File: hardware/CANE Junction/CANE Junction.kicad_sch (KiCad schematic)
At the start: 19 parts, among them J101 Conn_02x05_Odd_Even, SW101 SW_Push, U101 NCP163ASN330T1G, U102 NCP163ASN330T1G, U103 XMSM0G3507SDGS28R

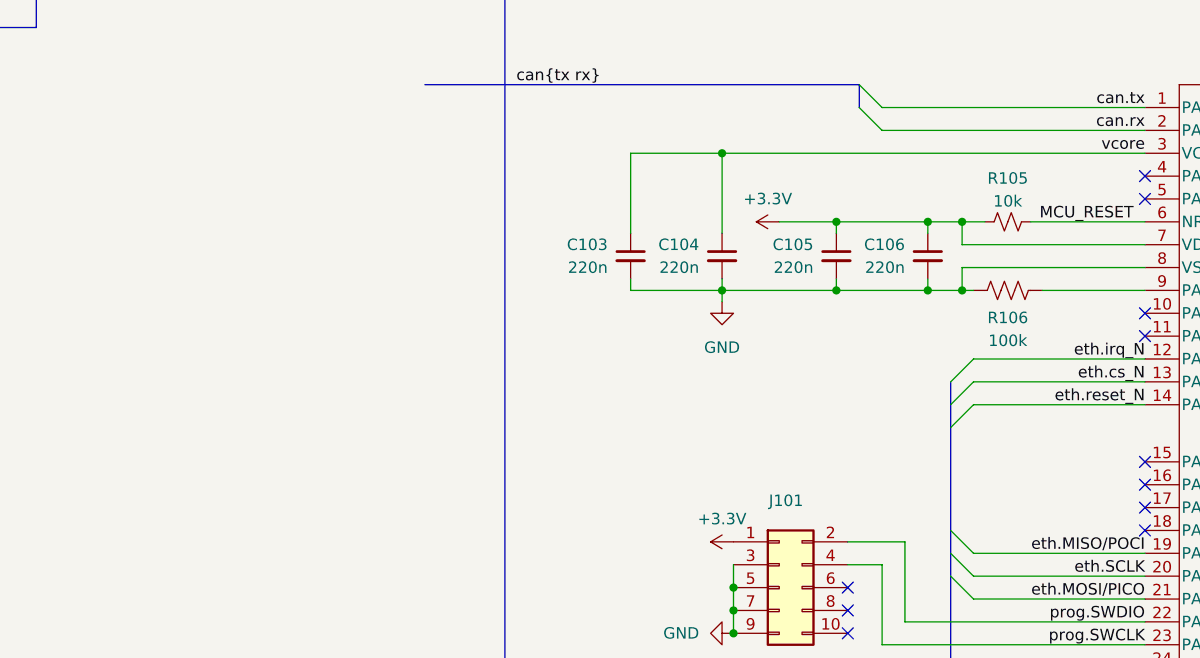
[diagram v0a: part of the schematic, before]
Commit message: pt
mspm0g3519 is da goat. 2 can interfaces but gate kept by bga footprint and high pin count qfps. one must manually port it. started the port, 2 out of 100 pins done :D :D u love ultra librariariairan
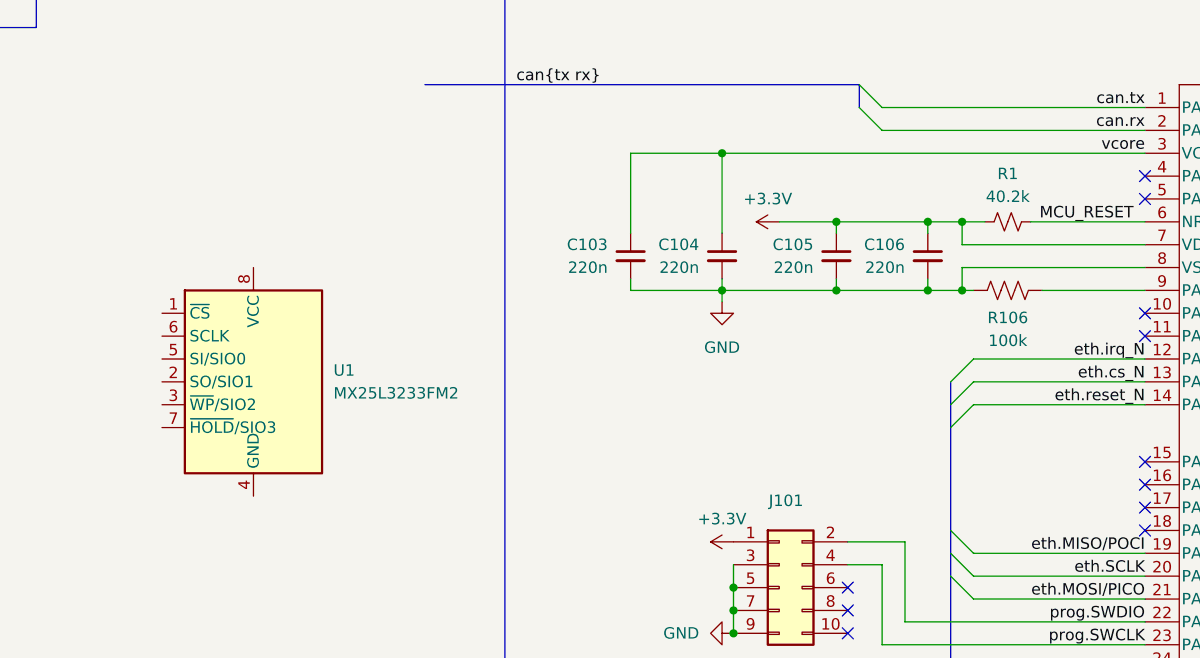
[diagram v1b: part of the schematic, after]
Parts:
- removed R105: 10k, Resistor_SMD:R_0805_2012Metric_Pad1.20x1.40mm_HandSolder, symbol Device:R_Small_US
- added R1: 40.2k, Resistor_SMD:R_0805_2012Metric_Pad1.20x1.40mm_HandSolder, symbol Device:R_Small_US
- added U1: MX25L3233FM2, Package_SO:SOIC-8_3.9x4.9mm_P1.27mm, symbol Memory_Flash:MX25L3233FM2
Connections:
- net +3.3V: now also R1.2
- net MCU_RESET: now also R1.1
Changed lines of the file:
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@@
+	(symbol
+		(lib_id "Device:R_Small_US")
+		(at 209.55 90.17 270)
+		(unit 1)
+		(exclude_from_sim no)
+		(in_bom yes)
+		(on_board yes)
+		(dnp no)
+		(property "Reference" "R1"
+			(at 209.55 84.836 90)
+			(effects
+				(font
+					(size 1.27 1.27)
+				)
+			)
+		)
+		(property "Value" "40.2k"
+			(at 209.55 87.376 90)
+			(effects
+				(font
+					(size 1.27 1.27)
+				)
+			)
+		)
+		(property "Footprint" "Resistor_SMD:R_0805_2012Metric_Pad1.20x1.40mm_HandSolder"
+			(at 209.55 90.17 0)
+			(effects
+				(font
+					(size 1.27 1.27)
+				)
+				(hide yes)
+			)
+		)
+		(property "Datasheet" ""
+			(at 209.55 90.17 0)
+			(effects
+				(font
+					(size 1.27 1.27)
+				)
+				(hide yes)
+			)
+		)
+		(property "Description" "Resistor, US symbol"
+			(at 209.55 90.17 0)
+			(effects
+				(font
+					(size 1.27 1.27)
+				)
+				(hide yes)
+			)
+		)
+		(property "mouser" "https://www.mouser.com/ProductDetail/KOA-Speer/RK73H2ATTD4022F?qs=sGAEpiMZZMvdGkrng054txknJuA7M8fa4wn7EqIHwNI%3D"
+			(at 209.55 90.17 0)
+			(effects
+				(font
+					(size 1.27 1.27)
+				)
+				(hide yes)
+			)
+		)
+		(property "specs" "40.2k ohm, 250mW, 1%, 150V, 100ppm, -55C, +155C"
+			(at 209.55 90.17 0)
+			(effects
+				(font
+					(size 1.27 1.27)
+				)
+				(hide yes)
+			)
+		)
+		(property "unit x10" "0.02"
+			(at 209.55 90.17 0)
+			(effects
+				(font
+					(size 1.27 1.27)
+				)
+				(hide yes)
+			)
+		)
+		(property "unit x1" "0.1"
+			(at 209.55 90.17 0)
+			(effects
+				(font
+					(size 1.27 1.27)
+				)
+				(hide yes)
+			)
+		)
+		(property "Mouser Part Number" ""
+			(at 209.55 90.17 0)
+			(effects
+				(font
+					(size 1.27 1.27)
+				)
+				(hide yes)
+			)
+		)
+		(property "Field10" ""
+			(at 209.55 90.17 0)
+			(effects
+				(font
+					(size 1.27 1.27)
+				)
+				(hide yes)
+			)
+		)
+		(pin "2"
+		)
+		(pin "1"
+		)
+		(instances
+			(project "CANE Junction"
+				(path "/20ac6af0-79b5-4ba6-aad3-75081d02c913"
+					(reference "R1")
+					(unit 1)
+				)
+			)
+		)
+	)
 	(symbol
 		(lib_id "Device:R_Small_US")
@@
 	)
 	(symbol
-		(lib_id "Device:R_Small_US")
-		(at 209.55 90.17 270)
+		(lib_id "Memory_Flash:MX25L3233FM2")
+		(at 125.73 107.95 0)
 		(unit 1)
 		(exclude_from_sim no)
@@
 		(on_board yes)
 		(dnp no)
-		(property "Reference" "R105"
-			(at 209.55 85.344 90)
-			(effects
-				(font
-					(size 1.27 1.27)
-				)
-			)
-		)
-		(property "Value" "10k"
-			(at 209.55 87.884 90)
-			(effects
-				(font
-					(size 1.27 1.27)
-				)
-			)
-		)
-		(property "Footprint" "Resistor_SMD:R_0805_2012Metric_Pad1.20x1.40mm_HandSolder"
-			(at 209.55 90.17 0)
-			(effects
-				(font
-					(size 1.27 1.27)
-				)
-				(hide yes)
-			)
-		)
-		(property "Datasheet" "~"
-			(at 209.55 90.17 0)
-			(effects
-				(font
-					(size 1.27 1.27)
-				)
-				(hide yes)
-			)
-		)
-		(property "Description" "Resistor, US symbol"
-			(at 209.55 90.17 0)
-			(effects
-				(font
-					(size 1.27 1.27)
-				)
-				(hide yes)
-			)
-		)
-		(property "Sim.Device" ""
-			(at 209.55 90.17 0)
-			(effects
-				(font
-					(size 1.27 1.27)
-				)
-				(hide yes)
-			)
-		)
-		(property "Sim.Type" ""
-			(at 209.55 90.17 0)
-			(effects
-				(font
-					(size 1.27 1.27)
-				)
-				(hide yes)
-			)
-		)
-		(property "mouser" "https://www.mouser.com/ProductDetail/YAGEO/AC0805FR-7W10KL?qs=sGAEpiMZZMvdGkrng054t4v35oYz4BJEgsNpGKlk%252BQ%2FXDjzK07E4tA%3D%3D"
-			(at 209.55 90.17 0)
-			(effects
-				(font
-					(size 1.27 1.27)
-				)
-				(hide yes)
-			)
-		)
-		(property "specs" "10k , 250mW, 150V, 1%, 100ppm, -55C, +155C"
-			(at 209.55 90.17 0)
-			(effects
-				(font
-					(size 1.27 1.27)
-				)
-				(hide yes)
-			)
-		)
-		(property "unit x10" "0.015"
-			(at 209.55 90.17 0)
-			(effects
-				(font
-					(size 1.27 1.27)
-				)
-				(hide yes)
-			)
-		)
-		(property "unit x1" "0.1"
-			(at 209.55 90.17 0)
-			(effects
-				(font
-					(size 1.27 1.27)
-				)
-				(hide yes)
-			)
-		)
-		(property "Sim.Pins" ""
-			(at 209.55 90.17 0)
-			(effects
-				(font
-					(size 1.27 1.27)
-				)
-				(hide yes)
-			)
-		)
-		(property "note" ""
-			(at 209.55 90.17 0)
-			(effects
-				(font
-					(size 1.27 1.27)
-				)
-				(hide yes)
-			)
-		)
-		(property "Mouser Part Number" "603-AC0805FR-7W10KL "
-			(at 209.55 90.17 0)
-			(effects
-				(font
-					(size 1.27 1.27)
-				)
-				(hide yes)
-			)
-		)
-		(property "Field10" ""
-			(at 209.55 90.17 90)
-			(effects
-				(font
-					(size 1.27 1.27)
-				)
-				(hide yes)
-			)
+		(fields_autoplaced yes)
+		(property "Reference" "U1"
+			(at 134.62 106.6799 0)
+			(effects
+				(font
+					(size 1.27 1.27)
+				)
+				(justify left)
+			)
+		)
+		(property "Value" "MX25L3233FM2"
+			(at 134.62 109.2199 0)
+			(effects
+				(font
+					(size 1.27 1.27)
+				)
+				(justify left)
+			)
+		)
+		(property "Footprint" "Package_SO:SOIC-8_3.9x4.9mm_P1.27mm"
+			(at 125.73 123.19 0)
+			(effects
+				(font
+					(size 1.27 1.27)
+				)
+				(hide yes)
+			)
+		)
+		(property "Datasheet" "https://www.macronix.com/Lists/Datasheet/Attachments/8933/MX25L3233F,%203V,%2032Mb,%20v1.7.pdf"
+			(at 125.73 125.476 0)
+			(effects
+				(font
+					(size 1.27 1.27)
+				)
+				(hide yes)
+			)
+		)
+		(property "Description" "32-Mbit, 3V (2.65V-3.6V) SPI Serial Flash Memory, SOIC-8 (SOP-8, 208 mil)"
+			(at 125.73 107.95 0)
+			(effects
+				(font
+					(size 1.27 1.27)
+				)
+				(hide yes)
+			)
+		)
+		(property "mouser" "https://www.mouser.com/ProductDetail/Infineon-Technologies/FM25L16B-GTR?qs=pA5MXup5wxFR0QOlB39bHA%3D%3D"
+			(at 125.73 107.95 0)
+			(effects
+				(font
+					(size 1.27 1.27)
+				)
+				(hide yes)
+			)
+		)
+		(property "unit x1" "1.67"
+			(at 125.73 107.95 0)
+			(effects
+				(font
+					(size 1.27 1.27)
+				)
+				(hide yes)
+			)
+		)
+		(property "unit x10" "1.57"
+			(at 125.73 107.95 0)
+			(effects
+				(font
+					(size 1.27 1.27)
+				)
+				(hide yes)
+			)
+		)
+		(pin "8"
+		)
+		(pin "7"
+		)
+		(pin "1"
 		)
 		(pin "2"
 		)
-		(pin "1"
+		(pin "3"
+		)
+		(pin "4"
+		)
+		(pin "6"
+		)
+		(pin "5"
 		)
 		(instances
-			(project "CANE Junction"
+			(project ""
 				(path "/20ac6af0-79b5-4ba6-aad3-75081d02c913"
-					(reference "R105")
+					(reference "U1")
 					(unit 1)
 				)

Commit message: mmm
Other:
- note added: "TODO - voltage monitoring on each interface - order the mspm0g3519 evaluation board as well - order bga breakout for the YCJ footprint, test"
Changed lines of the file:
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@@
+		)
+	)
+	(text "TODO\n- voltage monitoring on each interface\n- order the mspm0g3519 evaluation board as well\n- order bga breakout for the YCJ footprint, test"
+		(exclude_from_sim no)
+		(at 60.452 -4.826 0)
+		(effects
+			(font
+				(size 5.08 5.08)
+				(thickness 1.016)
+				(bold yes)
+			)
+			(justify left)
 		)
 	)
@@
 	(wire
 		(pts
+			(xy 204.47 95.25) (xy 224.79 95.25)
+		)
+		(stroke
+			(width 0)
+			(type default)
+		)
+	)
+	(wire
+		(pts
 			(xy 167.64 82.55) (xy 177.8 82.55)
 		)
@@
 		)
 		(stroke
-			(width 0)
-			(type default)
-		)
-	)
-	(wire
-		(pts
-			(xy 224.79 95.25) (xy 204.47 95.25)
-		)
-		(stroke

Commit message: bga it is
ycj footpritn too small for jlc, ztl one instead but have the solder-skill maxxing and hope & pray
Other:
- note added: "WATCH - micro bga my belovid, YCJ gets released ~june 2026"
- note removed: "TODO - voltage monitoring on each interface - order the mspm0g3519 evaluation board as well - order bga breakout for the YCJ footprint, test"
- moved on the sheet: U1

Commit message: shuffle master 2000
nearing terminal shuffle . main components in, awaiting general and layout tie ins
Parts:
- removed C101, C106: 220n, Capacitor_SMD:C_0805_2012Metric_Pad1.18x1.45mm_HandSolder, symbol Device:C_Small
- removed R1: 40.2k, Resistor_SMD:R_0805_2012Metric_Pad1.20x1.40mm_HandSolder, symbol Device:R_Small_US
- removed R101, R102: 2, Resistor_SMD:R_0805_2012Metric_Pad1.20x1.40mm_HandSolder, symbol Device:R_Small_US
- removed R106: 100k, Resistor_SMD:R_1206_3216Metric_Pad1.30x1.75mm_HandSolder, symbol Device:R_US
- removed U101: NCP163ASN330T1G, Package_TO_SOT_SMD:SOT-23-5_HandSoldering, symbol Regulator_Linear:NCP163ASN330T1G
- removed U103: XMSM0G3507SDGS28R, zzLocalLibraries-Footprints:VSSOP28_DGS_TEX-M, symbol zzLocalLibrary:XMSM0G3507SDGS28R
- added BZ1: Buzzer, Buzzer_Beeper:MagneticBuzzer_ProSignal_ABI-009-RC, symbol Device:Buzzer
- added C107: 220n, Capacitor_SMD:C_0805_2012Metric_Pad1.18x1.45mm_HandSolder, symbol Device:C_Small
- added D1, D2: SD0805S020S1R0, Diode_SMD:D_0805_2012Metric_Pad1.15x1.40mm_HandSolder, symbol Device:D_Schottky_Small
- added IC1: PAM8904QJER, zzLocalLibraries-Footprints:QFN50P300X300X65-17N-D, symbol zzLocalLibrary:PAM8904QJER
- added R2: 40.2k, Resistor_SMD:R_0805_2012Metric_Pad1.20x1.40mm_HandSolder, symbol Device:R_Small_US
- added R3: 100k, Resistor_SMD:R_0805_2012Metric_Pad1.20x1.40mm_HandSolder, symbol Device:R_Small_US
- added U2: XMSPM0G3519SPMR, zzLocalLibraries-Footprints:LQFP64_PM_TEX-M, symbol zzLocalLibrary:XMSPM0G3519SPMR
- added U3: TMP110D, Package_SON:Texas_X2SON-5_0.8x0.8mm_P0.48mm_RoutingVia, symbol Sensor_Temperature:TMP110D
- U102: value NCP163ASN330T1G -> NCP114ASN180T2G; mouser https://www.mouser.com/ProductDetail/onsemi/NCP115ASN330T2G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 -> https://www.mouser.com/ProductDetail/onsemi/NCP114ASN180T2G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; note (none) -> careful of built in active discharge
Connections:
- net MCU_RESET is gone; now on net GND: SW101.2
- net +3.3V: now also U102.5 (VOUT), C107.2, R2.1, U2.40 (VDD); no longer C105.1
- net CAN interface 1/5v: now also D1.2 (A)
- net CAN interface 2/5v: now also D2.2 (A); no longer U102.1 (VIN), U102.3 (EN)
- net GND: now also C107.1, R3.1, U2.41 (VSS); no longer SW101.1
- net prog.SWCLK: now also U2.13 (PA20)
- net prog.SWDIO: now also U2.12 (PA19)
- net vcore: no longer names the net of C103.1, C104.1
- net vcore: now also U2.32 (VCORE)
- new net: R2.2, SW101.1, U2.38 (NRST)
- new net: R3.2, U2.42 (PA2)
- new net: C105.1, D1.1 (K), D2.1 (K), U102.1 (VIN), U102.3 (EN)
- new net can0.RX: U2.6 (PA13)
- new net can0.TX: U2.5 (PA12)
- new net can0.term: U2.4 (PB16)
- new net can1.RX: U2.21 (PB22)
- new net can1.TX: U2.20 (PB21)
- new net can1.term: U2.19 (PB20)
- no-connect marks 14 -> 3
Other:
- sheet Ethernet ports: added none; removed LED Vdd
- note removed: "MCU"
- title: BeeMS Master Board (A) -> CANE Junciton
- moved on the sheet: C102, C103, C104, J101, SW101, U1, U102

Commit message: CANE put together and seemingly not exploding
meow meow meow
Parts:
- removed D101: green, LED_SMD:LED_0805_2012Metric_Pad1.15x1.40mm_HandSolder, symbol Device:LED_Small
- removed J101: Conn_02x05_Odd_Even, Connector_PinHeader_1.27mm:PinHeader_2x05_P1.27mm_Vertical_SMD, symbol Connector_Generic:Conn_02x05_Odd_Even
- removed R104: 2.4k, Resistor_SMD:R_0805_2012Metric_Pad1.20x1.40mm_HandSolder, symbol Device:R_Small_US
- removed U3: TMP110D, Package_SON:Texas_X2SON-5_0.8x0.8mm_P0.48mm_RoutingVia, symbol Sensor_Temperature:TMP110D
- added C108, C109: 220n, Capacitor_SMD:C_0805_2012Metric_Pad1.18x1.45mm_HandSolder, symbol Device:C_Small
- added C825, C826, C827: 100n, Capacitor_SMD:C_0805_2012Metric_Pad1.18x1.45mm_HandSolder, symbol Device:C_Small
- added H1, H2, H3, H4: MountingHole, MountingHole:MountingHole_4.3mm_M4_ISO7380, symbol Mechanical:MountingHole
- added J3: programming, Connector_PinHeader_2.54mm:PinHeader_1x03_P2.54mm_Vertical, symbol Connector_Generic:Conn_01x03
- added J4: UART, Connector_PinHeader_2.54mm:PinHeader_1x03_P2.54mm_Vertical, symbol Connector_Generic:Conn_01x03
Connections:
- net +3.3V: now also IC1.15 (VIN), U1.3 (~{WP}/SIO2), U1.7 (~{HOLD}/SIO3), U1.8 (VCC), C108.1, C109.2
- net GND: now also D102.1 (K), IC1.6 (GND), U1.4 (GND), U2.63 (PB11), C108.2, C109.1, C825.1, J3.1 (Pin_1), J4.1 (Pin_1); no longer R103.2
- net can0.term: now also U2.7 (PA14); no longer U2.4 (PB16)
- net eth.MISO/POCI: now also U2.59 (PB7)
- net eth.MOSI/PICO: now also U2.60 (PB8)
- net eth.SCLK: now also U2.61 (PB9)
- net eth.cs_N: now also U2.62 (PB10)
- net eth.reset_N: now also U2.58 (PB6)
- net prog.SWCLK: now also J3.2 (Pin_2)
- net prog.SWDIO: now also J3.3 (Pin_3)
- net at U2.33 (PA0): now also R103.1
- net SECD.MISO/POCI: now reaches U2.44 (PA4)
- net SECD.MISO/POCI: now also U1.2 (SO/SIO1)
- net SECD.MOSI/PICO: now reaches U2.45 (PA5)
- net SECD.MOSI/PICO: now also U1.5 (SI/SIO0)
- net SECD.SCLK: now reaches U2.46 (PA6)
- net SECD.SCLK: now also U1.6 (SCLK)
- net SECD.cs_fr: now reaches U2.48 (PB1)
- net SECD.cs_fr: now also U1.1 (~{CS})
- net uart1.TX: now reaches U2.54 (PA8)
- net uart1.TX: now also J4.2 (Pin_2)
- net uart1.RX: now reaches U2.55 (PA9)
- net uart1.RX: now also J4.3 (Pin_3)
- net buzzer.pwm: now reaches U2.64 (PB12)
- net buzzer.pwm: now also IC1.3 (DIN)
- net buzzer.pm1: now reaches U2.8 (PA15)
- net buzzer.pm1: now also IC1.1 (CPM1)
- net buzzer.pm2: now reaches U2.9 (PA16)
- net buzzer.pm2: now also IC1.2 (CPM2)
- net at BZ1.1 (+): now also IC1.9 (VO1)
- net at BZ1.2 (-): now also IC1.7 (VO2)
- net at IC1.10 (CN2): now also C826.1
- net at IC1.11 (CP1): now also C827.2
- net at IC1.13 (VOUT): now also C825.2
- net at IC1.14 (CP2): now also C826.2
- net at IC1.5 (CN1): now also C827.1
- net led.sched: no longer names the net of D102.2 (A)
- net led.sched: now also R103.2
- no-connect marks 3 -> 40
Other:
- sheet CAN interface 1: file CAN interface.kicad_sch -> CAN interface 1.kicad_sch
- sheet CAN interface 2: file CAN interface.kicad_sch -> CAN interface 2.kicad_sch
- note added: "WATCH - micro bga my belovid, swap the MCU to use the YCJ footprint when it gets released ~june 2026,"
- note removed: "Scheduler running"
- note removed: "WATCH - micro bga my belovid, YCJ gets released ~june 2026"
- note removed: "indicator 1"
- moved on the sheet: BZ1, C102, C103, C104, C105, C107, D1, D102, D2, IC1, R103, R2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
